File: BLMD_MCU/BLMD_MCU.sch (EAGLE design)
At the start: 2 parts

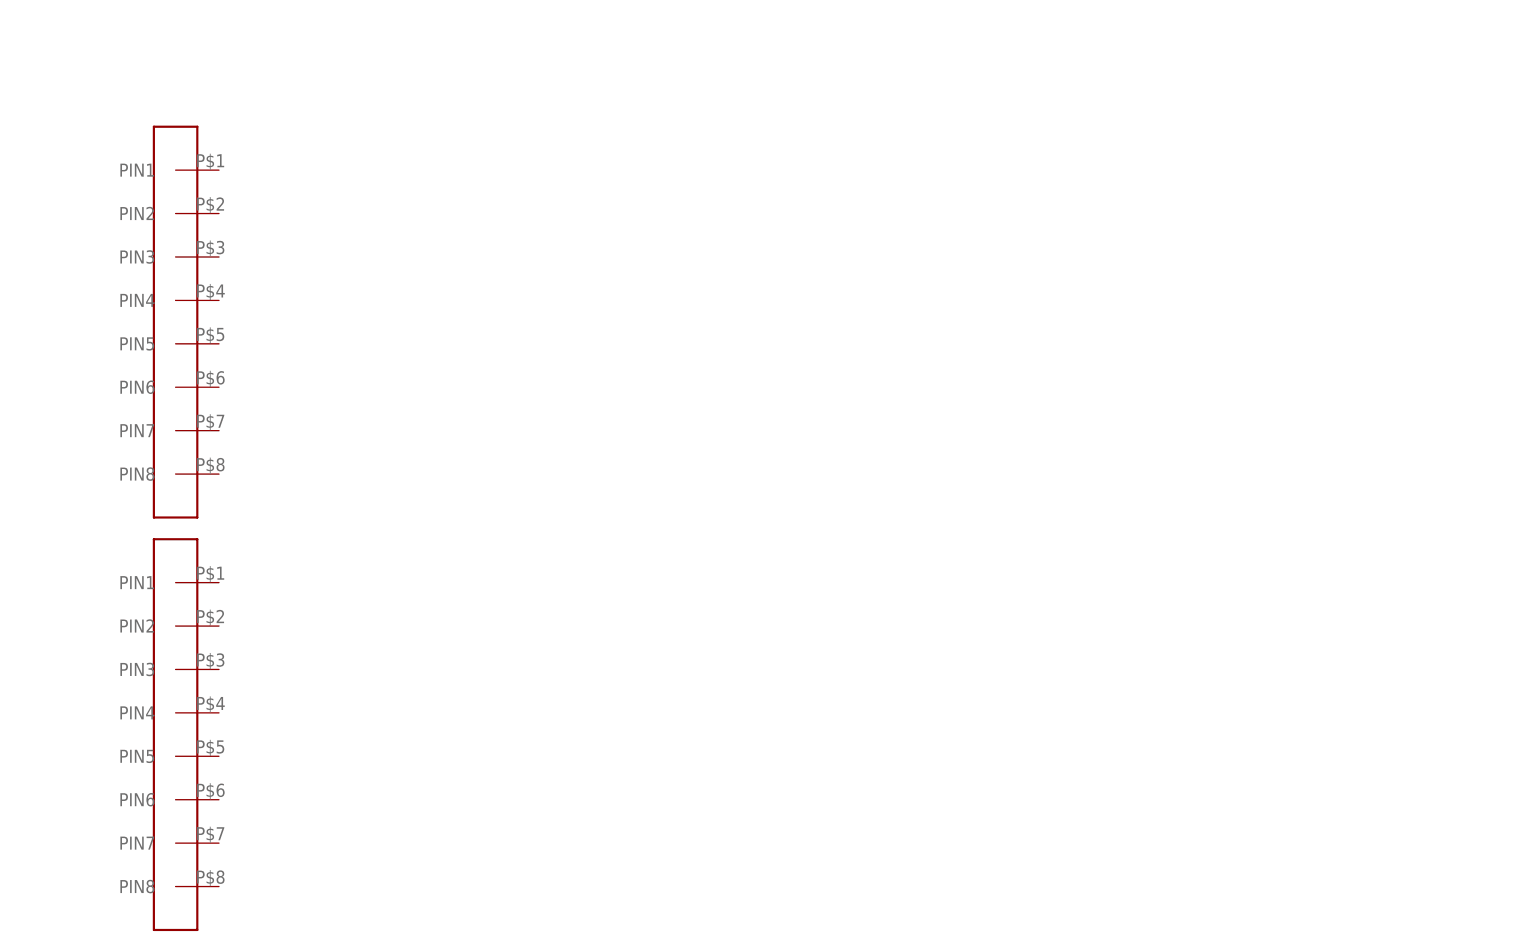
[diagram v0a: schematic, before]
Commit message: UVW結線のふっとぷりんと追加、新ガーバーファイル追加
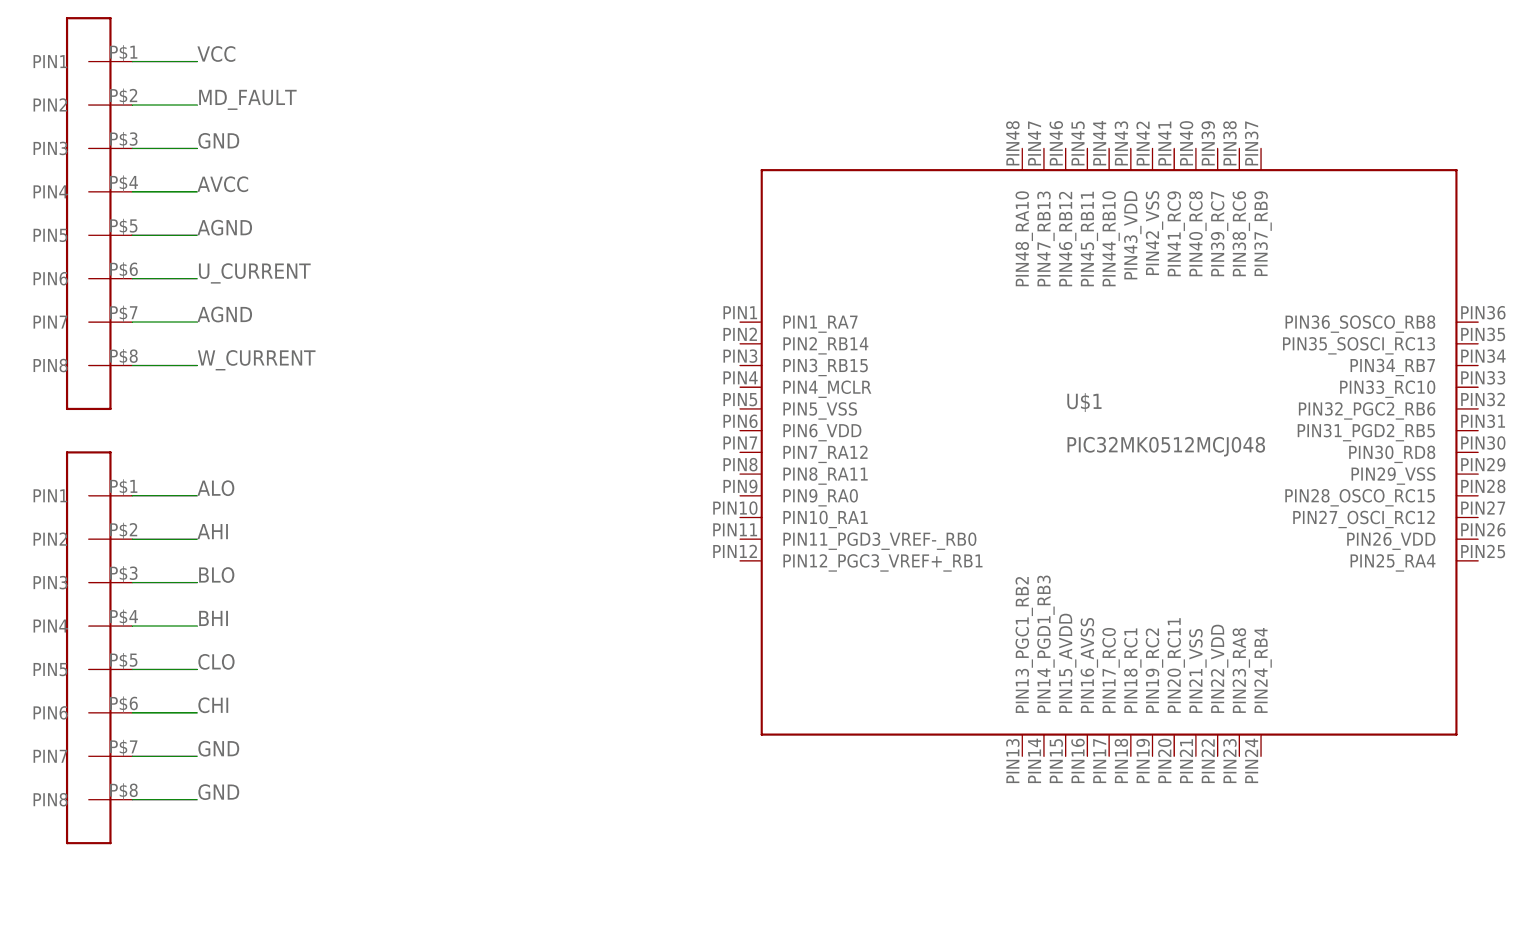
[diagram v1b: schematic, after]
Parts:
- added U$1: PIC32MK0512MCJ048, user_ic:PIC32MK0512MCJ048
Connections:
- new net AGND: CON2.PIN5, CON2.PIN7
- new net AHI: CON1.PIN2
- new net ALO: CON1.PIN1
- new net AVCC: CON2.PIN4
- new net BHI: CON1.PIN4
- new net BLO: CON1.PIN3
- new net CHI: CON1.PIN6
- new net CLO: CON1.PIN5
- new net GND: CON1.PIN7, CON1.PIN8, CON2.PIN3
- new net MD_FAULT: CON2.PIN2
- new net U_CURRENT: CON2.PIN6
- new net VCC: CON2.PIN1
- new net W_CURRENT: CON2.PIN8
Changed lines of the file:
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@@
 <part name="CON1" library="user_conector" deviceset="JQ_S8P" device=""/>
 <part name="CON2" library="user_conector" deviceset="JQ_S8P" device=""/>
+<part name="U$1" library="user_ic" deviceset="PIC32MK0512MCJ048" device=""/>
 </parts>
 <sheets>
@@
 </plain>
 <instances>
-<instance part="CON1" gate="G$1" x="25.4" y="73.66" smashed="yes" rot="R270"/>
-<instance part="CON2" gate="G$1" x="25.4" y="25.4" smashed="yes" rot="R270"/>
+<instance part="CON1" gate="G$1" x="15.24" y="35.56" smashed="yes" rot="R270"/>
+<instance part="CON2" gate="G$1" x="15.24" y="86.36" smashed="yes" rot="R270"/>
+<instance part="U$1" gate="G$1" x="132.08" y="60.96" smashed="yes">
+<attribute name="NAME" x="129.54" y="63.5" size="1.778" layer="95"/>
+<attribute name="VALUE" x="129.54" y="58.42" size="1.778" layer="96"/>
+</instance>
 </instances>
 <busses>
 </busses>
 <nets>
+<net name="ALO" class="0">
+<segment>
+<pinref part="CON1" gate="G$1" pin="PIN1"/>
+<wire x1="20.32" y1="53.34" x2="27.94" y2="53.34" width="0.1524" layer="91"/>
+<label x="27.94" y="53.34" size="1.778" layer="95"/>
+</segment>
+</net>
+<net name="AHI" class="0">
+<segment>
+<pinref part="CON1" gate="G$1" pin="PIN2"/>
+<wire x1="20.32" y1="48.26" x2="27.94" y2="48.26" width="0.1524" layer="91"/>
+<label x="27.94" y="48.26" size="1.778" layer="95"/>
+</segment>
+</net>
+<net name="BLO" class="0">
+<segment>
+<pinref part="CON1" gate="G$1" pin="PIN3"/>
+<wire x1="20.32" y1="43.18" x2="27.94" y2="43.18" width="0.1524" layer="91"/>
+<label x="27.94" y="43.18" size="1.778" layer="95"/>
+</segment>
+</net>
+<net name="BHI" class="0">
+<segment>
+<pinref part="CON1" gate="G$1" pin="PIN4"/>
+<wire x1="20.32" y1="38.1" x2="27.94" y2="38.1" width="0.1524" layer="91"/>
+<label x="27.94" y="38.1" size="1.778" layer="95"/>
+</segment>
+</net>
+<net name="CLO" class="0">
+<segment>
+<pinref part="CON1" gate="G$1" pin="PIN5"/>
+<wire x1="20.32" y1="33.02" x2="27.94" y2="33.02" width="0.1524" layer="91"/>
+<label x="27.94" y="33.02" size="1.778" layer="95"/>
+</segment>
+</net>
+<net name="CHI" class="0">
+<segment>
+<pinref part="CON1" gate="G$1" pin="PIN6"/>
+<wire x1="20.32" y1="27.94" x2="27.94" y2="27.94" width="0.1524" layer="91"/>
+<label x="27.94" y="27.94" size="1.778" layer="95"/>
+</segment>
+</net>
+<net name="VCC" class="0">
+<segment>
+<pinref part="CON2" gate="G$1" pin="PIN1"/>
+<wire x1="20.32" y1="104.14" x2="27.94" y2="104.14" width="0.1524" layer="91"/>
+<label x="27.94" y="104.14" size="1.778" layer="95"/>
+</segment>
+</net>
+<net name="MD_FAULT" class="0">
+<segment>
+<pinref part="CON2" gate="G$1" pin="PIN2"/>
+<wire x1="20.32" y1="99.06" x2="27.94" y2="99.06" width="0.1524" layer="91"/>
+<label x="27.94" y="99.06" size="1.778" layer="95"/>
+</segment>
+</net>
+<net name="GND" class="0">
+<segment>
+<pinref part="CON2" gate="G$1" pin="PIN3"/>
+<wire x1="20.32" y1="93.98" x2="27.94" y2="93.98" width="0.1524" layer="91"/>
+<label x="27.94" y="93.98" size="1.778" layer="95"/>
+</segment>
+<segment>
+<pinref part="CON1" gate="G$1" pin="PIN7"/>
+<wire x1="20.32" y1="22.86" x2="27.94" y2="22.86" width="0.1524" layer="91"/>
+<label x="27.94" y="22.86" size="1.778" layer="95"/>
+</segment>
+<segment>
+<pinref part="CON1" gate="G$1" pin="PIN8"/>
+<wire x1="20.32" y1="17.78" x2="27.94" y2="17.78" width="0.1524" layer="91"/>
+<label x="27.94" y="17.78" size="1.778" layer="95"/>
+</segment>
+</net>
+<net name="AVCC" class="0">
+<segment>
+<pinref part="CON2" gate="G$1" pin="PIN4"/>
+<wire x1="20.32" y1="88.9" x2="27.94" y2="88.9" width="0.1524" layer="91"/>
+<label x="27.94" y="88.9" size="1.778" layer="95"/>
+</segment>
+</net>
+<net name="AGND" class="0">
+<segment>
+<pinref part="CON2" gate="G$1" pin="PIN5"/>
+<wire x1="27.94" y1="83.82" x2="20.32" y2="83.82" width="0.1524" layer="91"/>
+<label x="27.94" y="83.82" size="1.778" layer="95"/>
+</segment>
+<segment>
+<pinref part="CON2" gate="G$1" pin="PIN7"/>
+<wire x1="20.32" y1="73.66" x2="27.94" y2="73.66" width="0.1524" layer="91"/>
+<label x="27.94" y="73.66" size="1.778" layer="95"/>
+</segment>
+</net>
+<net name="U_CURRENT" class="0">
+<segment>
+<pinref part="CON2" gate="G$1" pin="PIN6"/>
+<wire x1="20.32" y1="78.74" x2="27.94" y2="78.74" width="0.1524" layer="91"/>
+<label x="27.94" y="78.74" size="1.778" layer="95"/>
+</segment>
+</net>
+<net name="W_CURRENT" class="0">
+<segment>
+<pinref part="CON2" gate="G$1" pin="PIN8"/>
+<wire x1="20.32" y1="68.58" x2="27.94" y2="68.58" width="0.1524" layer="91"/>
+<label x="27.94" y="68.58" size="1.778" layer="95"/>
+</segment>
+</net>
 </nets>
 </sheet>

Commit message: MCU側回路図を作成
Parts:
- added C1, C12, C2, C4, C5: 0.1u, rcl:C-EUC1608
- added C10: 2.2u, rcl:C-EUC1608
- added C11, C8, C9: 1u, rcl:C-EUC1608
- added C3: (no value), rcl:C-EUC1608
- added C6: 100u, rcl:C-EUC3216
- added C7: 10u, rcl:C-EUC1608
- added CN1: 7810-8P8C, user_conector:7810-8P8C
- added CON3: (no value), user_conector:XH_4P
- added CON4: (no value), user_conector:XH_6P
- added CON5: (no value), user_conector:XH_3P
- added D1, D2, D3: SBR2U30P1, user_diode:SMD_DAIOD
- added IC1: ADP151AUJZ, user_ic:ADP151AUJZ
- added IC2: (no value), user_ic:NJW1616T
- added IC3: AZ1117CH, user_ic:AZ1117CH
- added IC4: (no value), user_ic:MCP2562MCP2561-SN
- added JP1: (no value), pinhead:PINHD-1X2
- added L1: 47u, user_rcl:L_SMD_INDUCTOR
- added LED1: RGB_LED, user_leds:RGB_LED
- added OSC1: 20MHz, user_osc:CSTN#
- added R1, R6: 10k, user_rcl:R_REG
- added R10, R11, R12, R16, R17, R18, R2, R3, R4, R5: (no value), user_rcl:R_REG
- added R13, R14, R15: 47k, user_rcl:R_REG
- added R7: 3.3k, user_rcl:R_REG
- added R8: 0, user_rcl:R_REG
- added R9: 120, user_rcl:R_REG
- added SW1: (no value), user_swich:DIPSW4
- added U$2: TAKUTOSUITTI2, user_swich:TAKUTOSUITTI2
- added U$4: XH_2P, user_conector:XH_2P
- added U$5: CUHS20S30, user_diode:CUHS20S30
- added U$6: FDC6305, user_tr_fet_igbt:FDC6305
- added U$7: SOT23_NFET, user_tr_fet_igbt:SOT23_NFET
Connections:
- new net +5V: C11.1, C12.1, C6.1, C8.1, D1.C, IC1.1_VIN, IC1.3_EN, IC3.PIN3_INPUT, IC4.VDD, L1.2, R6.2
- new net CANH: CN1.6, CON5.PIN1, IC4.CANH, JP1.1
- new net CANL: CN1.3, CON5.PIN2, IC4.CANL, R9.1
- new net CAN_RX: IC4.RXD, U$1.PIN25_RA4
- new net CAN_TX: IC4.TXD, U$1.PIN24_RB4
- new net FF1_LED: R14.1, U$1.PIN35_SOSCI_RC13, U$6.PIN1_G1
- new net FF2_LED: R15.1, U$1.PIN36_SOSCO_RB8, U$6.PIN3_G2
- new net HOME1: U$1.PIN19_RC2
- new net ID_1: R2.2, SW1.1, U$1.PIN1_RA7
- new net ID_2: R3.2, SW1.2, U$1.PIN48_RA10
- new net ID_3: R4.2, SW1.3, U$1.PIN47_RB13
- new net ID_4: R5.2, SW1.4, U$1.PIN46_RB12
- new net INDX1: U$1.PIN18_RC1
- new net MCLR: C1.1, CON4.PIN1, R1.1, U$1.PIN4_MCLR, U$2.PIN1
- new net N$1: R12.2, U$1.PIN8_RA11
- new net N$10: IC2.3_FB, R6.1, R7.2
- new net N$11: LED1.R_A, R16.2
- new net N$12: LED1.B_K, U$7.PIN2_D
- new net N$13: CON3.PIN1, D1.A
- new net N$14: LED1.G_K, U$6.PIN6_D1
- new net N$15: LED1.R_K, U$6.PIN4_D2
- new net N$16: D2.A, U$4.PIN1
- new net N$17: R13.1, R14.2, R15.2, U$7.PIN3_S
- new net N$18: CN1.4, D3.A
- new net N$2: R11.2, U$1.PIN10_RA1
- new net N$3: LED1.B_A, R18.2
- new net N$4: R10.2, U$1.PIN12_PGC3_VREF+_RB1
- new net N$5: OSC1.OUT, U$1.PIN27_OSCI_RC12
- new net N$6: OSC1.IN, U$1.PIN28_OSCO_RC15
- new net N$7: LED1.G_A, R17.2
- new net N$8: JP1.2, R9.2
- new net N$9: IC2.6_SW, L1.1, U$5.C
- new net PGC: CON4.PIN5, U$1.PIN13_PGC1_RB2
- new net PGD: CON4.PIN4, U$1.PIN14_PGD1_RB3
- new net QEA1: U$1.PIN17_RC0
- new net QEB1: U$1.PIN23_RA8
- new net QEICMP1: U$1.PIN3_RB15
- new net STAT_LED: R13.2, U$1.PIN31_PGD2_RB5, U$7.PIN1_G
- new net UART_RX: CON3.PIN2, U$1.PIN32_PGC2_RB6
- new net UART_TX: CON3.PIN3, U$1.PIN34_RB7
- new net V+: C7.1, CN1.5, D2.C, D3.C, IC2.4_SHDN, IC2.5_VIN
- net AGND: now also C8.2, C9.2, IC1.2_GND, R10.1, R11.1, R12.1, R8.2, U$1.PIN16_AVSS
- net AHI: now also U$1.PIN38_RC6
- net ALO: now also U$1.PIN39_RC7
- net AVCC: now also C9.1, IC1.5_VOUT, U$1.PIN15_AVDD
- net BHI: now also U$1.PIN40_RC8
- net BLO: now also U$1.PIN41_RC9
- net CHI: now also U$1.PIN44_RB10
- net CLO: now also U$1.PIN45_RB11
- net GND: now also C1.2, C10.2, C11.2, C12.2, C2.2, C3.2, C4.2, C5.2, C6.2, C7.2, CN1.7, CN1.8, CON3.PIN4, CON4.PIN3, CON5.PIN3, IC2.2_GND, IC3.PIN1_GND, IC4.STBY, IC4.VSS, OSC1.GND, R2.1, R3.1, R4.1, R5.1, R7.1, R8.1, U$1.PIN21_VSS, U$1.PIN29_VSS, U$1.PIN42_VSS, U$1.PIN5_VSS, U$2.PIN2, U$4.PIN2, U$5.A
- net MD_FAULT: now also U$1.PIN30_RD8
- net U_CURRENT: now also U$1.PIN11_PGD3_VREF-_RB0
- net VCC: now also C10.1, C2.1, C3.1, C4.1, C5.1, CON4.PIN2, IC3.PIN2_OUT, IC3.PIN4_OUT, IC4.VIO, R1.2, R16.1, R17.1, R18.1, SW1.5, SW1.6, SW1.7, SW1.8, U$1.PIN22_VDD, U$1.PIN26_VDD, U$1.PIN43_VDD, U$1.PIN6_VDD
- net W_CURRENT: now also U$1.PIN9_RA0
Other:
- note added: "1k ohom"
- note added: "47k ohom"
- note added: "CAN ID Configration"
- note added: "MCPWM"
- note added: "Shield to Anarog Signal Input"
- note added: "未実装"
- moved on the sheet: U$1

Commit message: 基板完成　ガーバーファイル追加
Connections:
- removed net N$17: R13.1, R14.2, R15.2, U$7.PIN3_S
- net GND: now also R13.1, R14.2, R15.2, U$7.PIN3_S
- net N$18: now also CN1.5
- net V+: no longer CN1.5
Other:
- note added: "Analog Power Supply"
- note added: "CAN Tra"
- note added: "Down Converter"
- note added: "ID Select DipSW"
- note added: "LED for Stat And FF"
- note added: "MCU Debug Interface"
- note added: "MCU Power Supply"
- note added: "MD Interface"
- note added: "Reset Circuit"
- note added: "Special CAN Interface"
- note added: "Special Power Supply"
- note added: "Standard CAN And Power Interface"
- note added: "UART Interface at 3.3V"
- moved on the sheet: C1, C10, C11, C12, C2, C3, C4, C5, C6, C7, C8, C9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

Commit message: ガーバーファイル追加
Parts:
- U$7: value SOT23_NFET -> AO3400A
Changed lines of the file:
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@@
 <part name="LED1" library="user_leds" deviceset="RGB_LED" device=""/>
 <part name="U$6" library="user_tr_fet_igbt" deviceset="FDC6305" device=""/>
-<part name="U$7" library="user_tr_fet_igbt" deviceset="SOT23_NFET" device=""/>
+<part name="U$7" library="user_tr_fet_igbt" deviceset="SOT23_NFET" device="" value="AO3400A"/>
 <part name="R13" library="user_rcl" deviceset="R_REG" device="" value="47k"/>
 <part name="R14" library="user_rcl" deviceset="R_REG" device="" value="47k"/>
@@
 <instance part="U$7" gate="G$1" x="81.28" y="73.66" smashed="yes">
 <attribute name="NAME" x="86.36" y="76.2" size="1.778" layer="95"/>
-<attribute name="VALUE" x="66.04" y="78.74" size="1.778" layer="96"/>
+<attribute name="VALUE" x="86.36" y="71.12" size="1.778" layer="96"/>
 </instance>
 <instance part="R13" gate="G$1" x="76.2" y="30.48" smashed="yes" rot="R90">
